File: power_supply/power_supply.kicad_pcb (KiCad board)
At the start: 2 copper layers, 5 parts, among them J1 Input, J2 Input

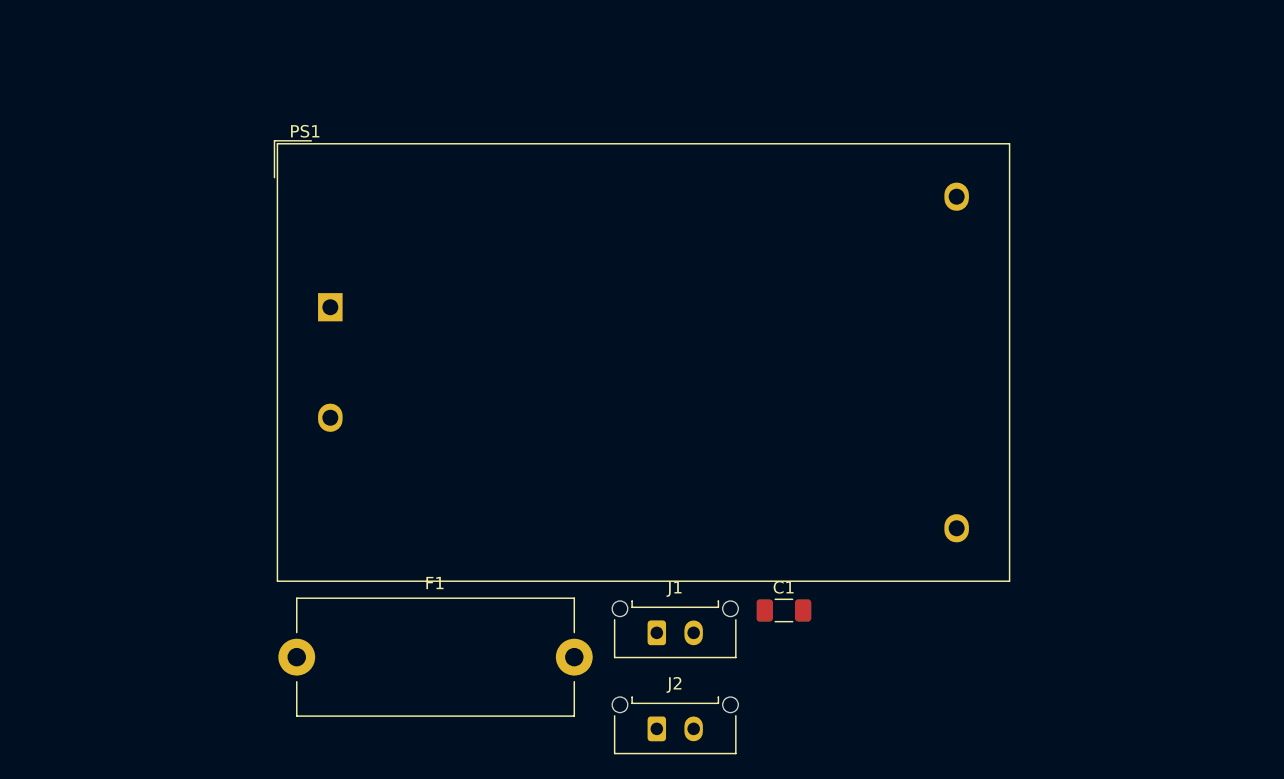
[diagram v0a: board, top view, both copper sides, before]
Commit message: update powersupply pcb
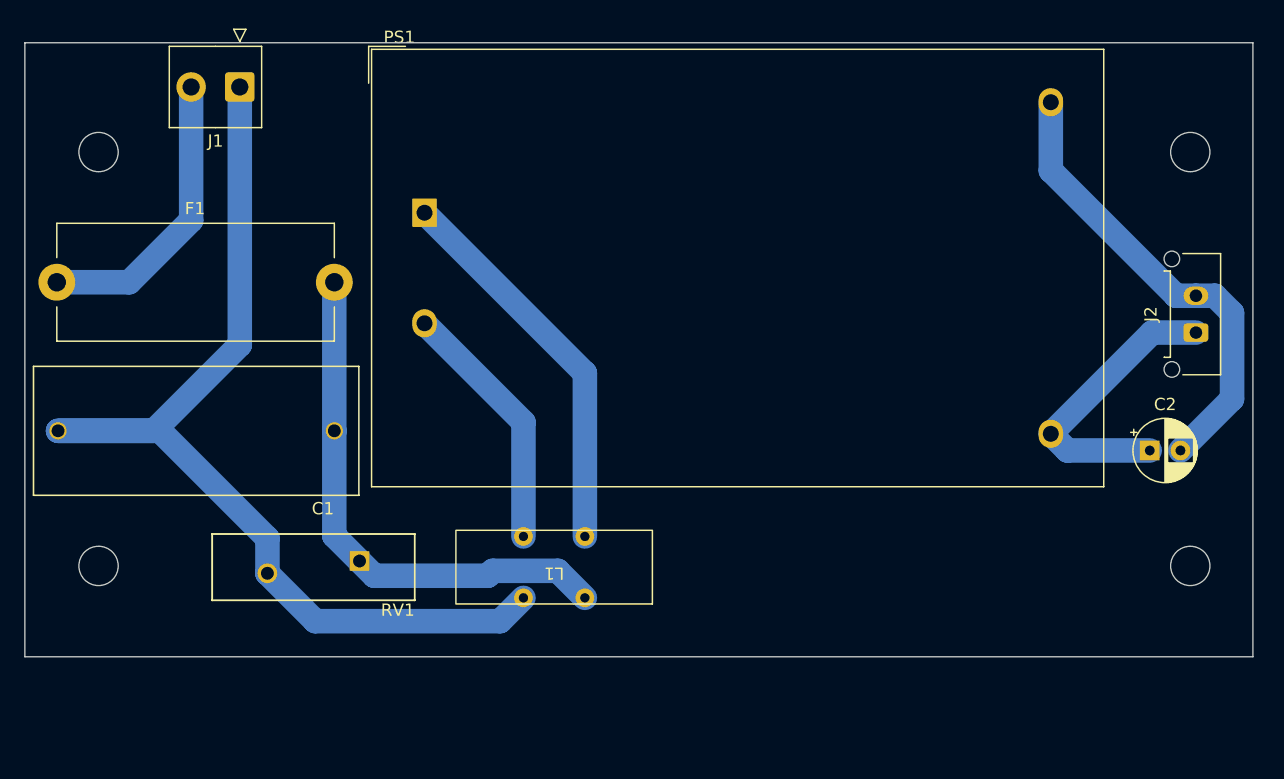
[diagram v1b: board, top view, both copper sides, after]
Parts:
- added C2: 100uF /6.3V, Capacitor_THT:CP_Radial_D5.0mm_P2.50mm, F.Cu at (181.1, 86.2)
- added L1: 10mH, PowerLibrary:IndRing, F.Cu at (132.6, 95.7)
- added RV1: 10D561K, eec:Bourns_Inc.-MOV-14D471K-MFG, F.Cu at (113.0, 95.7)
- added hole1: MountingHole_3.2mm_M3, MountingHole:MountingHole_3.2mm_M3, F.Cu at (184.3, 95.6)
- added hole1: MountingHole_3.2mm_M3, MountingHole:MountingHole_3.2mm_M3, F.Cu at (95.5, 61.9)
- added hole1: MountingHole_3.2mm_M3, MountingHole:MountingHole_3.2mm_M3, F.Cu at (184.3, 61.9)
- added hole1: MountingHole_3.2mm_M3, MountingHole:MountingHole_3.2mm_M3, F.Cu at (95.5, 95.6)
- C1: footprint Capacitor_SMD:C_1206_3216Metric_Pad1.33x1.80mm_HandSolder -> B32023B3104K000:CAPRR2250W80L2650T1050H1650
- J1: footprint Connector_Molex:Molex_Micro-Fit_3.0_43650-0215_1x02_P3.00mm_Vertical -> Connector_TE-Connectivity:TE_826576-2_1x02_P3.96mm_Vertical
- moved J1 55.9 mm to (107.0, 56.6), turned to 180 degrees
- moved J2 54.5 mm to (184.8, 76.6), turned to 90 degrees
- moved C1 50.0 mm to (103.4, 84.6), turned to 180 degrees
- moved F1 36.2 mm to (92.0, 72.5)
- moved PS1 10.9 mm to (122.0, 66.8)
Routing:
- net Net-(J1-Pin_1): track 0.00 -> 85.5 mm
- net Net-(C1-Pad1): track 0.00 -> 43.5 mm
- net Net-(J2-Pin_2): track 0.00 -> 38.1 mm
- net Net-(PS1-AC/L): track 0.00 -> 31.8 mm
- net Net-(J1-Pin_2): track 0.00 -> 23.9 mm
- net Net-(J2-Pin_1): track 0.00 -> 23.9 mm
- net Net-(PS1-AC/N): track 0.00 -> 20.7 mm
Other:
- board outline added: 100 x 50 mm

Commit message: upd
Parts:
- moved J1 5.32 mm to (111.0, 60.1)
- moved PS1 3.04 mm to (122.5, 69.8)
- moved C2 2.52 mm to (183.4, 85.4)
- moved L1 0.86 mm to (133.1, 96.4)
- moved RV1 0.86 mm to (113.5, 96.4)
- moved F1 0.64 mm to (92.5, 72.9)
- moved J2 0.60 mm to (185.4, 76.6)
- moved C1 0.59 mm to (104.0, 84.4)
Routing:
- net Net-(J1-Pin_1): track 85.5 -> 73.9 mm
- net Net-(J2-Pin_1): track 23.9 -> 29.4 mm
- net Net-(PS1-AC/N): track 20.7 -> 18.4 mm
- net Net-(PS1-AC/L): track 31.8 -> 29.5 mm
- net Net-(J2-Pin_2): track 38.1 -> 36.3 mm
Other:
- board size 100 x 50 mm -> 100 x 45 mm
